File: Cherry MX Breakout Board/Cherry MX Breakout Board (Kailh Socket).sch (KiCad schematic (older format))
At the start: 3 parts, among them J1 Conn_01x06_Male, U1 Cherry_MX_RGB

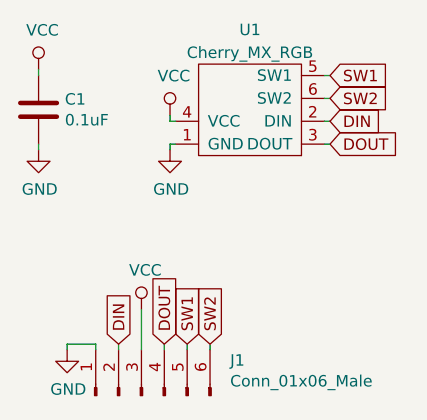
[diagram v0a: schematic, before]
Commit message: Fix footprints and PCBs
- removed silkscreen of Cherry MX and Kailh Socket
- LTST-A683CEGBW pinout and model was rotated which caused invalid connections
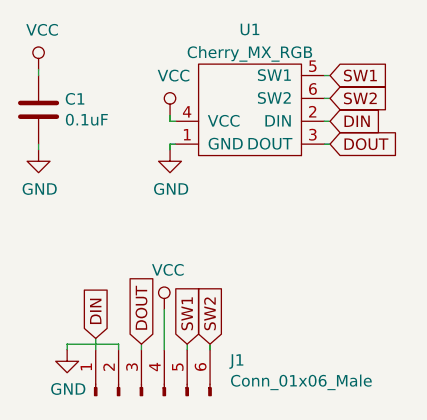
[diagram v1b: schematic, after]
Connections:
- net DIN: now also J1.1 (Pin_1); no longer J1.2 (Pin_2)
- net DOUT: now also J1.3 (Pin_3); no longer J1.4 (Pin_4)
- net GND: now also J1.2 (Pin_2); no longer J1.1 (Pin_1)
- net VCC: now also J1.4 (Pin_4); no longer J1.3 (Pin_3)
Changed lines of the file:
@@
 $EndComp
-Wire Wire Line
-	4975 4225 4975 4200
-Wire Wire Line
-	4975 4200 4850 4200
-Wire Wire Line
-	4850 4200 4850 4225
 Wire Wire Line
 	4725 3350 4725 3325
@@
 L power:VCC #PWR04
 U 1 1 5E285ED9
-P 5175 4050
-F 0 "#PWR04" H 5175 3900 50  0001 C CNN
-F 1 "VCC" H 5192 4223 50  0000 C CNN
-F 2 "" H 5175 4050 50  0001 C CNN
-F 3 "" H 5175 4050 50  0001 C CNN
-	1    5175 4050
+P 5275 4050
+F 0 "#PWR04" H 5275 3900 50  0001 C CNN
+F 1 "VCC" H 5292 4223 50  0000 C CNN
+F 2 "" H 5275 4050 50  0001 C CNN
+F 3 "" H 5275 4050 50  0001 C CNN
+	1    5275 4050
 	1    0    0    -1
 $EndComp
@@
 Text GLabel 5475 4200 1    50   Input ~ 0
 SW2
-Text GLabel 5075 4200 1    50   Input ~ 0
+Text GLabel 4975 4175 1    50   Input ~ 0
 DIN
-Text GLabel 5275 4200 1    50   Input ~ 0
+Text GLabel 5175 4200 1    50   Input ~ 0
 DOUT
 Wire Wire Line
@@
 Wire Wire Line
 	5375 4225 5375 4200
-Wire Wire Line
-	5275 4225 5275 4200
 $Comp
 L Device:C C1
@@
 	5075 4225 5075 4200
 Wire Wire Line
-	5175 4050 5175 4225
+	4850 4200 4850 4225
+Wire Wire Line
+	4850 4200 5075 4200
+Wire Wire Line
+	4975 4225 4975 4175
+Wire Wire Line
+	5175 4225 5175 4200
+Wire Wire Line
+	5275 4050 5275 4225
 $EndSCHEMATC
